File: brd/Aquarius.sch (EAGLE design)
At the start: 35 parts, among them IC1 74123D, J2 DS18B20, J4 GSM/GPS, U1 DHT22, U2 DS3231SN, X1 Conn BNC : pH, X2 Conn BNC : Dissolved Oxygen, X3 Conn BNC : Conductivity, X4 Batt.1, X5 Batt.2

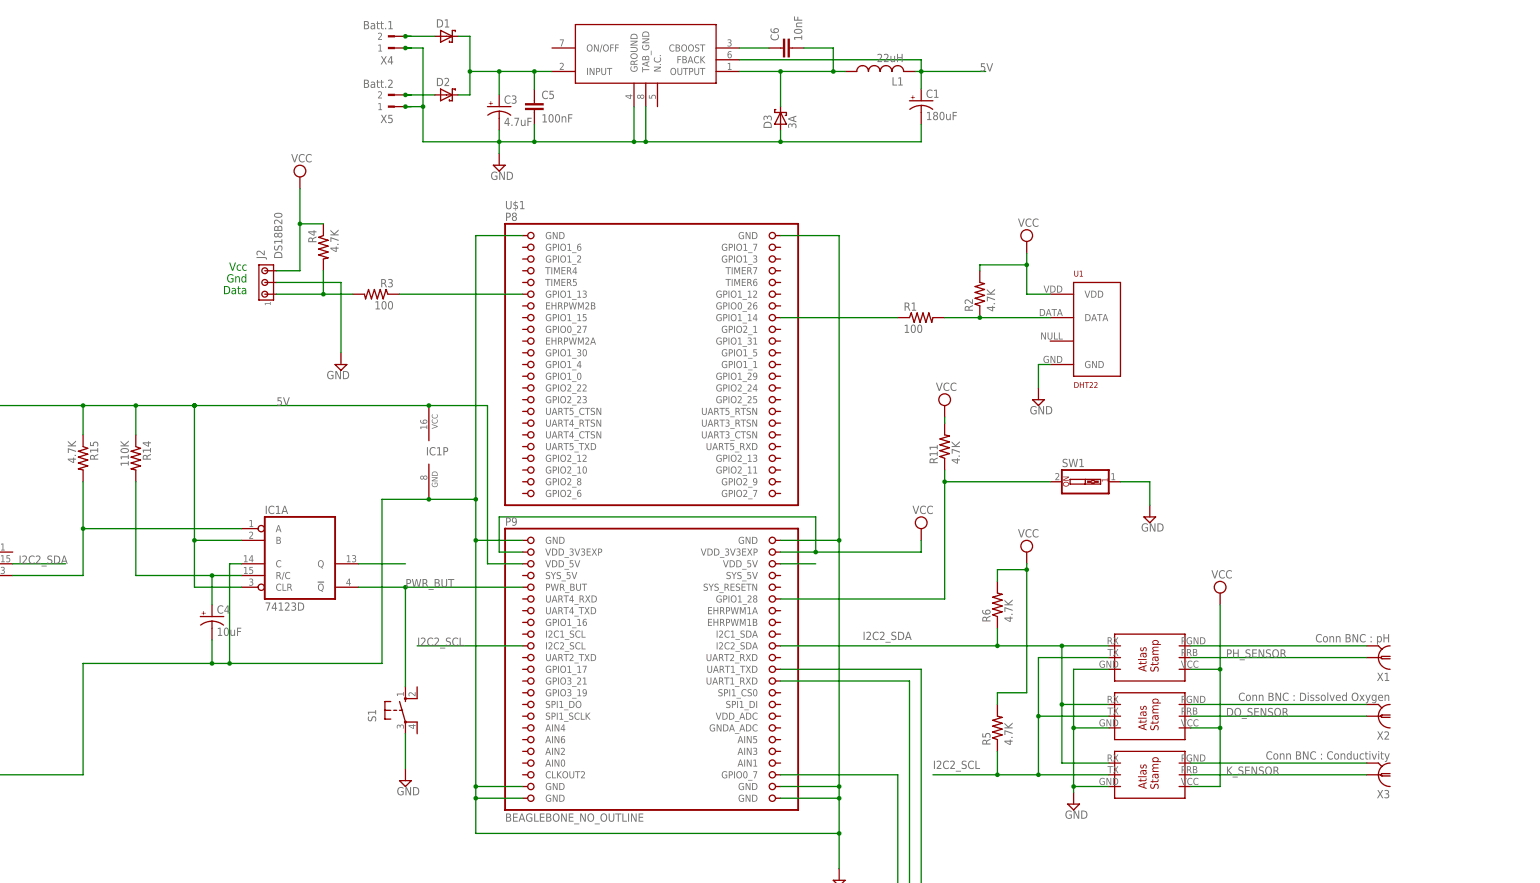
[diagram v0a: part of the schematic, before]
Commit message: PCB Update and modified name of Atlas driver cpp's
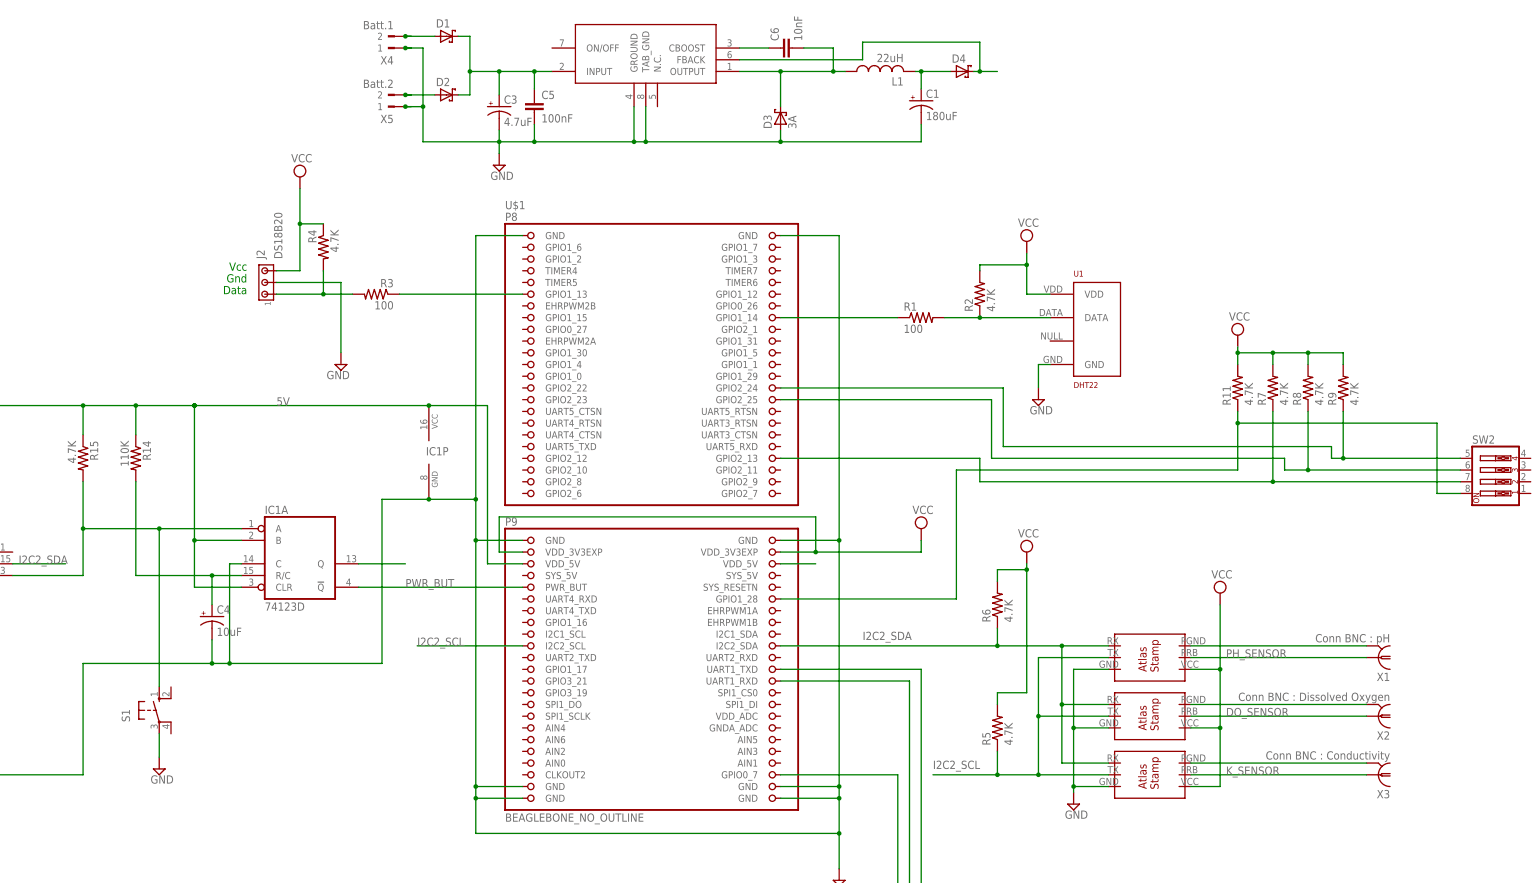
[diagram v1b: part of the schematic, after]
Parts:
- removed SW1: (no value), special:SW_DIP-1
- added D4: (no value), diode:SCHOTTKY-DIODEDO201T15
- added R7, R8, R9: 4.7K, adafruit:R-US_R0805
- added SW2: (no value), special:SW_DIP-4
- D1, D2, D3: device adafruit:SCHOTTKY-DIODECB417-15 -> diode:SCHOTTKY-DIODEDO201T15
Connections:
- new net N$16: C1.+, D4.A, L1.2
- new net N$18: R11.1, SW2.8, U$1.GPIO1_28
- new net N$19: R8.1, SW2.6, U$1.GPIO2_25
- new net N$21: R9.1, SW2.5, U$1.GPIO2_24
- net 5V: now also D4.C; no longer C1.+, L1.2
- net GND: no longer SW1.1
- net INT: now also S1.S
- net N$7: now also R7.1, SW2.7, U$1.GPIO2_13; no longer R11.1, SW1.2, U$1.GPIO1_28
- net PWR_BUT: no longer S1.S
- net VCC: now also R7.2, R8.2, R9.2
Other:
- moved on the sheet: R11, S1

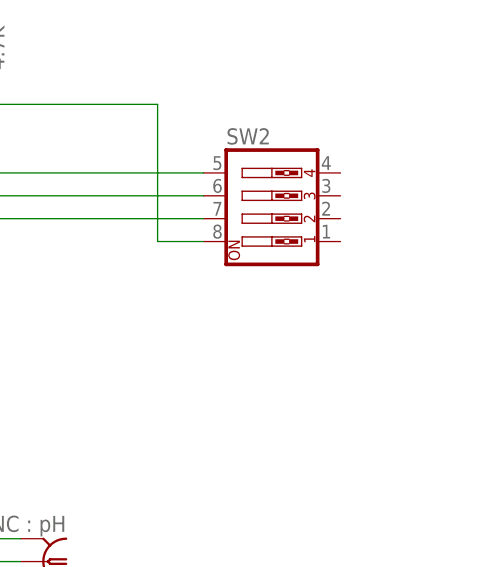
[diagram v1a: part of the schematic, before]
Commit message: Ajout de ground sur le schema
Préparation a une 2eime version du PCB
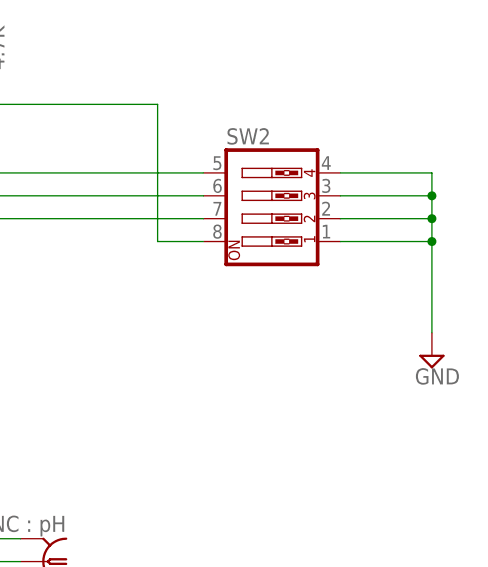
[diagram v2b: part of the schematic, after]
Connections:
- removed net N$1: U$1.VDD_5V@2
- net 5V: now also U$1.VDD_5V@2
- net GND: now also SW2.1, SW2.2, SW2.3, SW2.4
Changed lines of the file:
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@@
 <part name="R8" library="adafruit" deviceset="R-US_" device="R0805" value="4.7K"/>
 <part name="R9" library="adafruit" deviceset="R-US_" device="R0805" value="4.7K"/>
+<part name="SUPPLY7" library="supply2" deviceset="GND" device=""/>
 </parts>
 <sheets>
@@
 <instance part="R8" gate="G$1" x="160.02" y="81.28" rot="R90"/>
 <instance part="R9" gate="G$1" x="167.64" y="81.28" rot="R90"/>
+<instance part="SUPPLY7" gate="GND" x="218.44" y="45.72"/>
 </instances>
 <busses>
@@
 <junction x="-35.56" y="142.24"/>
 </segment>
+<segment>
+<pinref part="SW2" gate="A" pin="1"/>
+<pinref part="SUPPLY7" gate="GND" pin="GND"/>
+<wire x1="208.28" y1="58.42" x2="218.44" y2="58.42" width="0.1524" layer="91"/>
+<wire x1="218.44" y1="58.42" x2="218.44" y2="48.26" width="0.1524" layer="91"/>
+<pinref part="SW2" gate="A" pin="2"/>
+<wire x1="208.28" y1="60.96" x2="218.44" y2="60.96" width="0.1524" layer="91"/>
+<wire x1="218.44" y1="60.96" x2="218.44" y2="58.42" width="0.1524" layer="91"/>
+<junction x="218.44" y="58.42"/>
+<pinref part="SW2" gate="A" pin="3"/>
+<wire x1="208.28" y1="63.5" x2="218.44" y2="63.5" width="0.1524" layer="91"/>
+<wire x1="218.44" y1="63.5" x2="218.44" y2="60.96" width="0.1524" layer="91"/>
+<junction x="218.44" y="60.96"/>
+<pinref part="SW2" gate="A" pin="4"/>
+<wire x1="208.28" y1="66.04" x2="218.44" y2="66.04" width="0.1524" layer="91"/>
+<wire x1="218.44" y1="66.04" x2="218.44" y2="63.5" width="0.1524" layer="91"/>
+<junction x="218.44" y="63.5"/>
+</segment>
 </net>
 <net name="N$3" class="0">
@@
 <junction x="88.9" y="149.86"/>
 </segment>
+<segment>
+<pinref part="U$1" gate="G$1" pin="VDD_5V@2"/>
+<wire x1="53.34" y1="43.18" x2="45.72" y2="43.18" width="0.1524" layer="91"/>
+</segment>
 </net>
 <net name="PWR_BUT" class="0">
@@
 </segment>
 </net>
-<net name="N$1" class="0">
-<segment>
-<pinref part="U$1" gate="G$1" pin="VDD_5V@2"/>
-<wire x1="53.34" y1="43.18" x2="45.72" y2="43.18" width="0.1524" layer="91"/>
-</segment>
-</net>
